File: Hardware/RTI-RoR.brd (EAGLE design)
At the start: 80 x 71.1 mm, 31 parts, among them IC2 74LVC244

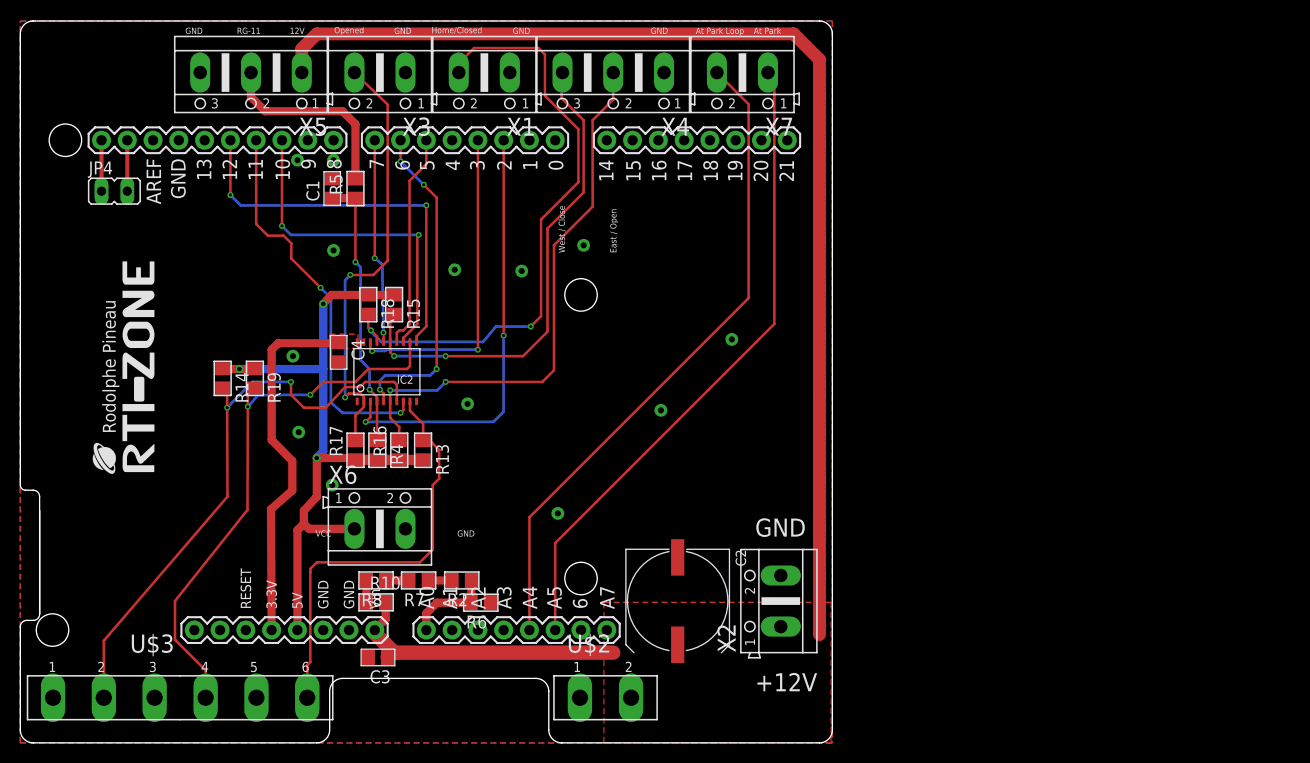
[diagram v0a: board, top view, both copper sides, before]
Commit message: Use the same board as the dome.
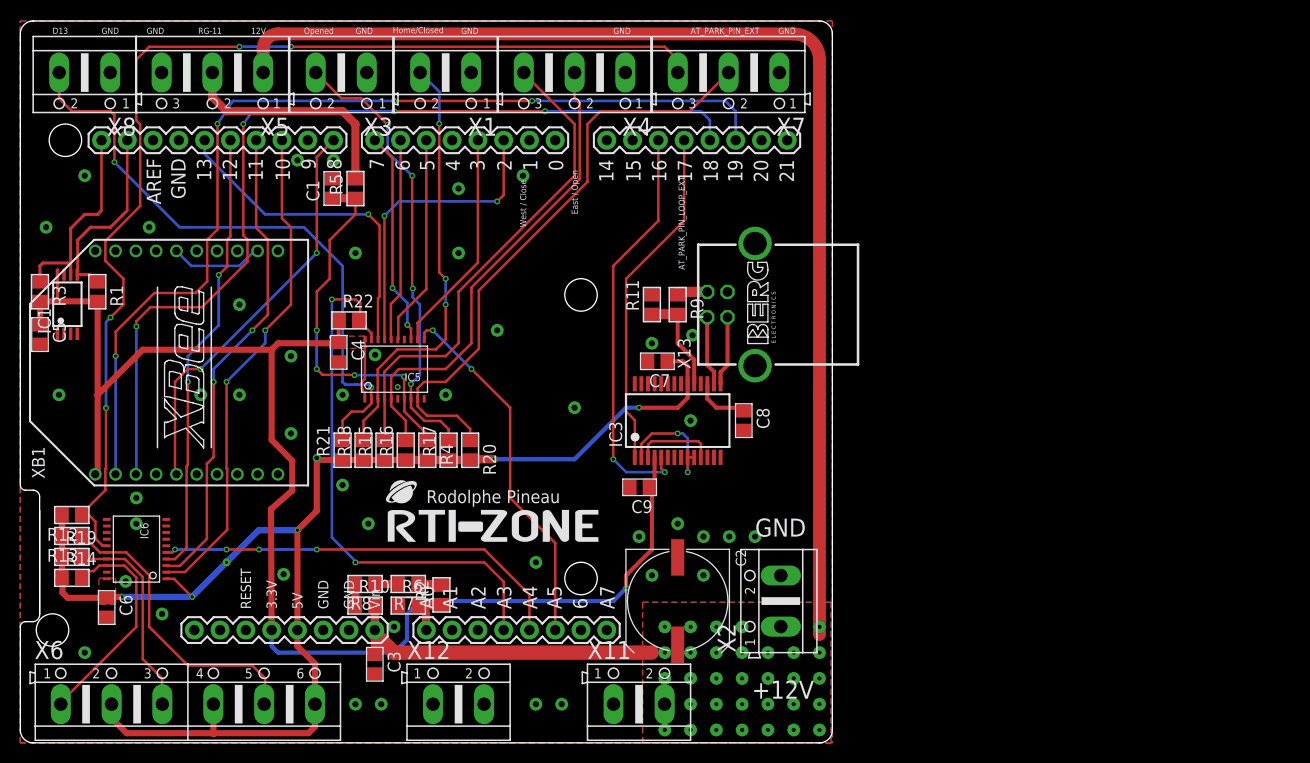
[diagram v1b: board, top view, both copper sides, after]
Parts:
- removed JP4: (no value), jumper:JP1
- removed U$2: STL-140-2, rti:STL-140-2
- removed U$3: STL-140-6, rti:STL-140-6
- added C5, C6, C7, C8, C9: 100nF, rti:C0805
- added IC1: 24AA128ST, microchip:TSSOP8
- added IC3: FT232RL, ftdichip:SSOP28
- added IC6: 74ABT245, rti:TSSOP20
- added R1, R3: 1K, rti:R0805
- added R11: 10K, rti:R0805
- added R12, R20, R21, R22, R9: 4.7K, rti:R0805
- added X11, X12, X8: (no value), con-ptr500:AK500/2
- added X13: PN61729-S, con-berg:PN61729-S
- added XB1: XBEE, maxstream:XBEE
- IC5: value 74LVC244 -> 74LVC245
- R13, R14, R19: value 1K -> 4.7K
- X6: device con-ptr500:AK500/2 -> con-ptr500:AK500/6
- X7: device con-ptr500:AK500/2 -> con-ptr500:AK500/3
- moved R13 35.6 mm to (5.08, 20.4), turned to 180 degrees
- moved X6 25.6 mm to (16.5, 3.81)
- moved R19 25.2 mm to (5.08, 18.3), turned to 0 degrees
- moved R14 24.6 mm to (5.08, 16.3), turned to 0 degrees
- moved U$4 24.0 mm to (36.2, 19.8), turned to 0 degrees
- moved R15 14.4 mm to (35.9, 28.8), turned to 90 degrees
- moved R18 14.4 mm to (33.8, 28.8), turned to 90 degrees
- moved R17 9.18 mm to (42.2, 28.8)
- moved R6 7.15 mm to (38.2, 13.5), turned to 0 degrees
- moved R4 4.92 mm to (40.1, 28.8)
- moved X1 3.81 mm to (41.9, 66.0)
- moved X4 3.81 mm to (54.6, 66.0)
- moved X5 3.81 mm to (18.9, 66.0)
- moved X3 3.81 mm to (31.6, 66.0)
- moved R2 2.46 mm to (41.5, 14.6), turned to 90 degrees
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- renumbered IC2 to IC5
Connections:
- removed net 13: PCB1.13
- removed net LOW_POWER: PCB1.4
- removed net N$8: JP4.2, PCB1.SDA1
- new net AT_PARK_PIN_EXT: IC5.P$9, R20.1, X7.2
- new net AT_PARK_PIN_LOOP_EXT: IC6.P$15, R12.1, X7.3
- new net BUF_EN: IC5.P$19, PCB1.A3, R22.2
- new net D13: IC5.P$18, PCB1.13
- new net D13_EXT: IC5.P$2, R21.2, X8.2
- new net DTR_DSR_DCD: IC3.10, IC3.2, IC3.9
- new net N$1: IC3.19, R11.1, R9.2
- new net N$4: IC5.P$14
- new net N$9: XB1.12, XB1.16
- new net RTS_CTS: IC3.11, IC3.3
- new net RX2: IC3.1, PCB1.17
- new net SCL: IC1.6, PCB1.SCL1, R3.1
- new net SDA: IC1.5, PCB1.SDA1, R1.1
- new net TX2: IC3.5, PCB1.16
- new net USBDM: IC3.16, X13.2
- new net USBDP: IC3.15, X13.3
- new net USB_VCC: R9.1, X13.1
- new net XBEE_DIN: PCB1.18, XB1.3
- new net XBEE_DOUT: PCB1.19, XB1.2
- net +12V: now also X11.2; no longer U$2.2
- net 3.3V: now also C5.1, C9.1, IC1.8, IC3.4, IC5.P$1, R1.2, R22.1, R3.2, XB1.1
- net AT_PARK_PIN: now also IC5.P$11; no longer X7.1
- net AT_PARK_PIN_LOOP: now also IC6.P$5; no longer X7.2
- net BUTTON_EAST_OPEN: now also IC5.P$15; no longer IC5.P$14
- net BUTTON_EAST_OPEN_5V: now also IC5.P$5; no longer IC5.P$6
- net BUTTON_WEST_CLOSE: now also IC5.P$16; no longer IC5.P$5
- net BUTTON_WEST_CLOSE_5V: now also IC5.P$4; no longer IC5.P$15
- net GND: now also C5.2, C6.2, C7.2, C8.2, C9.2, IC1.1, IC1.2, IC1.3, IC1.4, IC3.18, IC3.21, IC3.25, IC3.7, IC5.P$6, IC6.P$10, IC6.P$19, IC6.P$6, IC6.P$7, IC6.P$8, IC6.P$9, R11.2, X11.1, X12.1, X12.2, X13.4, X13.S1, X13.S2, X7.1, X8.1, XB1.10, XB1.9; no longer IC5.P$1, IC5.P$19, U$2.1, U$3.1, U$3.3, U$3.5, X6.2
- net HOME_SHUTTER_CLOSED: now also IC5.P$17; no longer IC5.P$3
- net HOME_SHUTTER_CLOSED_5V: now also IC5.P$3; no longer IC5.P$17
- net M_DIR: now also IC6.P$3; no longer IC5.P$8
- net M_DIR_5V: now also IC6.P$17, X6.3; no longer IC5.P$12, U$3.4
- net M_EN: now also IC6.P$2; no longer IC5.P$13
- net M_EN_5V: now also IC6.P$18, X6.1; no longer IC5.P$7, U$3.2
- net M_STEP: now also IC6.P$4; no longer IC5.P$11
- net M_STEP_5V: now also IC6.P$16, X6.5; no longer IC5.P$9, U$3.6
- net N$6: now also C8.1, IC3.17; no longer JP4.1, PCB1.SCL1
- net RG-11: now also IC5.P$13; no longer IC5.P$16
- net RG-11-IN_5V: now also IC5.P$7; no longer IC5.P$4
- net SHUTTER_OPENED: now also IC5.P$12; no longer IC5.P$18
- net SHUTTER_OPENED_5V: now also IC5.P$8; no longer IC5.P$2
- net VCC: now also C6.1, C7.1, IC3.20, IC6.P$1, IC6.P$20, R12.2, R20.2, R21.1, X6.2, X6.4, X6.6; no longer X6.1
- net XBEE_RESET: now also XB1.5
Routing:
- net 3.3V: track 36.4 -> 146.4 mm, vias 0 -> 1
- net AT_PARK_PIN_LOOP_EXT: track 0.00 -> 109.1 mm, vias 0 -> 4
- net XBEE_DOUT: track 0.00 -> 96.6 mm, vias 0 -> 4
- net XBEE_DIN: track 0.00 -> 91.2 mm, vias 0 -> 4
- net VCC: track 67.7 -> 135.2 mm, vias 3 -> 7
- net D13_EXT: track 0.00 -> 61.7 mm, vias 0 -> 2
- net AT_PARK_PIN_EXT: track 0.00 -> 59.3 mm
- net BUF_EN: track 0.00 -> 54.1 mm, vias 0 -> 2
- net TX2: track 0.00 -> 40.5 mm, vias 0 -> 2
- net XBEE_RESET: track 0.00 -> 40.2 mm, vias 0 -> 2
- net M_EN_5V: track 57.6 -> 21.9 mm, vias 2 -> 0
- net M_DIR_5V: track 54.6 -> 20.2 mm, vias 2 -> 0
- net RX2: track 0.00 -> 34.0 mm
- net D13: track 0.00 -> 32.8 mm, vias 0 -> 1
- net AT_PARK_PIN: track 64.1 -> 36.1 mm, vias 0 -> 2
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- added copper zone on layer 16, net +12V
- added copper zone on layer 1, net VCC
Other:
- outline, holes or cut-outs redrawn
- board text added: "AT_PARK_PIN_EXT"
- board text added: "AT_PARK_PIN_LOOP_EXT"
- board text added: "D13"
- board text removed: "At Park"
- board text removed: "At Park Loop"
- board text removed: "VCC"

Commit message: Re-base the code with the dome code
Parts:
- removed PCB1: ARDUINO_DUE_SHIELD_SHORT, arduino_shield:ARDUINO_DUE_SHIELD_SHORT
- removed R22, R9: 4.7K, rti:R0805
- removed X12: (no value), con-ptr500:AK500/2
- removed X6: (no value), con-ptr500:AK500/6
- added 25MHZ: CB3LV-OSCILATOR, rti:SMD-7050_4P
- added C10: 22nF, rcl:C0805
- added C11, C12, C14, C16, C17, C20: 100nF, rcl:C0805
- added C13, C18, C22: 10nF, rcl:C0805
- added C15, C21: 6.8nF, rcl:C0805
- added C19: 4.7uF, rcl:C0805
- added C25, C26: 10uF, rcl:C0805
- added FL1: BLM21AG121SN1D, BLM21AG121SN1D:L0805
- added IC4: REG1117, burr-brown:SOT223
- added J2: XT60PW-M, samacsys:XT60PWM
- added R23: 10 1%, rcl:R0805
- added R24, R25, R26, R27: 49.9 1%, rcl:R0805
- added R28, R29: 330, rcl:R0805
- added R30, R31, R32, R33, R34, R35, R36, R37, R38, R40: 4.7K, rcl:R0805
- added R39: 12.4K 1%, rcl:R0805
- added U$1: ARDUINO_DUE_SHIELD_FULL, arduino_shield:ARDUINO_DUE_SHIELD_FULL
- added U$2: MCP120T-270I_TT, MCP120T-270I_TT:SOT95P237X112-3N
- added U1: W5500, W5500:LQFP48
- added X10: (no value), rti:AK500/3
- added X9: J1011F21PNL, rti:J1011F21PNL
- C1, C3, C4, C5, C6, C7, C8, C9: device rti:C0805 -> rcl:C0805
- C2: device rti:UD-10X10_NICHICON -> rcl:UD-10X10_NICHICON
- IC1: device microchip:TSSOP8 -> rti:TSSOP8
- R1, R10, R11, R12, R13, R14, R15, R16, R17, R18, R19, R2, R20, R21, R3, R4, R5, R6, R7, R8: device rti:R0805 -> rcl:R0805
- X1, X11, X3, X8: device con-ptr500:AK500/2 -> rti:AK500/2
- X13: device con-berg:PN61729-S -> rti:PN61729-S
- X2: device con-ptr500:AK500/2 -> rti:AK500/3
- X4, X5, X7: device con-ptr500:AK500/3 -> rti:AK500/3
- XB1: device maxstream:XBEE -> rti:XBEE
- moved X2 66.7 mm to (8.99, 3.84), turned to 0 degrees
- moved IC3 45.5 mm to (106.7, 49.5)
- moved C7 45.5 mm to (104.7, 55.4)
- moved C8 45.5 mm to (113.2, 49.5)
- moved C9 45.5 mm to (102.9, 43.0)
- moved X13 45.5 mm to (114.3, 61.0)
- moved U$4 34.5 mm to (56.5, 47.8)
- moved R11 30.4 mm to (89.5, 56.7), turned to 0 degrees
- moved C2 29.5 mm to (94.0, 10.2)
- moved X11 21.6 mm to (82.5, 3.81)
- moved X7 1.02 mm to (68.8, 65.8)
- moved X4 0.85 mm to (53.8, 65.8)
- moved X1 0.64 mm to (41.3, 65.8)
- moved X3 0.38 mm to (31.3, 65.8)
- moved X5 0.24 mm to (18.8, 65.8)
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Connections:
- removed net BUF_EN: IC5.P$19, PCB1.A3, R22.2
- removed net N$1: IC3.19, R11.1, R9.2
- new net +3V3: 25MHZ.1, 25MHZ.4, C13.1, C16.1, C20.1, C26.1, C9.1, FL1.2, IC3.4, IC4.2, R28.2, R29.2, R30.2, R36.2, R37.2, R38.2, U1.28
- new net +5V: U$1.+5V@2
- new net ACT_LED: U1.27, X9.11
- new net AVDD: C11.1, C12.1, C14.1, C17.1, FL1.1, R23.2, R24.2, R25.2, U1.11, U1.15, U1.17, U1.21, U1.4, U1.8
- new net ETH_CS: U$1.52, U1.32
- new net ETH_RESET: R30.1, U$1.53, U1.37
- new net FTDI_RESET: IC3.19, R11.1, U$1.23
- new net INT_N: U$1.32, U1.36
- new net LINK_ACK: U1.25, X9.10
- new net N$10: R28.1, X9.12
- new net N$11: C15.2, X9.7
- new net N$12: C21.2, X9.8
- new net N$13: C10.1, R23.1, X9.3
- new net N$17: U1.26
- new net N$22: R31.1, U1.38
- new net N$23: R32.1, U1.39
- new net N$24: R33.1, U1.40
- new net N$25: R34.1, U1.41
- new net N$26: R35.1, U1.42
- new net N$27: R36.1, U1.43
- new net N$28: R37.1, U1.44
- new net N$29: R38.1, U1.45
- new net N$31: C19.2, U1.20
- new net N$32: U1.18
- new net N$33: C18.2, U1.22
- new net N$34: R39.1, U1.10
- new net N$35: R40.2, U1.23
- new net N$7: C22.1, R26.2, R27.2, X9.6
- new net N$8: R29.1, X9.9
- new net RESET: U$1.RESET, U$2.1
- new net RXN: C21.1, R26.1, U1.5
- new net RXP: C15.1, R27.1, U1.6
- new net SCLK: U$1.SCK, U1.33
- new net SDI: U$1.MISO, U1.34
- new net SDO: U$1.MOSI, U1.35
- new net TXN: R25.1, U1.1, X9.2
- new net TXP: R24.1, U1.2, X9.1
- new net XI: 25MHZ.3, U1.30
- new net XO: U1.31
- net +12V: now also C25.1, IC4.3, J2.2, U$1.VIN; no longer PCB1.VIN, X2.1
- net 3.3V: now also U$1.3.3V, U$2.2; no longer C9.1, IC3.4, PCB1.3.3V, R22.1
- net AT_PARK_PIN: now also U$1.A5; no longer PCB1.A5
- net AT_PARK_PIN_LOOP: now also U$1.A4; no longer PCB1.A4
- net BUTTON_EAST_OPEN: now also U$1.5; no longer PCB1.5
- net BUTTON_WEST_CLOSE: now also U$1.6; no longer PCB1.6
- net D13: now also U$1.13; no longer PCB1.13
- net GND: now also 25MHZ.2, C10.2, C11.2, C12.2, C13.2, C14.2, C16.2, C17.2, C18.1, C19.1, C20.2, C22.2, C25.2, C26.2, IC4.1, IC5.P$19, J2.1, R31.2, R32.2, R33.2, R34.2, R35.2, R39.2, R40.1, U$1.GND, U$1.GND., U$1.GND.., U$1.GND..., U$1.GND...., U$1.GND__, U$2.3, U1.14, U1.16, U1.19, U1.29, U1.3, U1.48, U1.9, X9.4, X9.5, X9.M1, X9.M2; no longer PCB1.GND, PCB1.GND., PCB1.GND.., X12.1, X12.2, X2.2
- net HOME_SHUTTER_CLOSED: now also U$1.2; no longer PCB1.2
- net M_DIR: now also U$1.11; no longer PCB1.11
- net M_DIR_5V: now also X2.3; no longer X6.3
- net M_EN: now also U$1.10; no longer PCB1.10
- net M_EN_5V: now also X2.1; no longer X6.1
- net M_STEP: now also U$1.12; no longer PCB1.12
- net M_STEP_5V: now also X10.2; no longer X6.5
- net RG-11: now also U$1.7; no longer PCB1.7
- net RX2: now also U$1.17; no longer PCB1.17
- net SCL: now also U$1.SCL1; no longer PCB1.SCL1
- net SDA: now also U$1.SDA1; no longer PCB1.SDA1
- net SHUTTER_OPENED: now also U$1.3; no longer PCB1.3
- net TX2: now also U$1.16; no longer PCB1.16
- net USB_VCC: no longer R9.1
- net VCC: now also U$1.+5V@1, U$1.+5V@3, U$1.+5V@4, X10.1, X10.3, X2.2; no longer PCB1.5V, X6.2, X6.4, X6.6
- net VPIN: now also U$1.A0; no longer PCB1.A0
- net XBEE_DIN: now also U$1.18; no longer PCB1.18
- net XBEE_DOUT: now also U$1.19; no longer PCB1.19
- net XBEE_RESET: now also U$1.8; no longer PCB1.8
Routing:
- net +3V3: track 0.00 -> 146.7 mm
- net AVDD: track 0.00 -> 96.8 mm, vias 0 -> 4
- net +12V: track 148.7 -> 239.2 mm
- net 3.3V: track 146.4 -> 90.1 mm, vias 1 -> 0
- net BUF_EN: track 54.1 -> 0.00 mm, vias 2 -> 0
- net ACT_LED: track 0.00 -> 48.9 mm, vias 0 -> 1
- net ETH_RESET: track 0.00 -> 46.6 mm, vias 0 -> 1
- net LINK_ACK: track 0.00 -> 45.7 mm, vias 0 -> 1
- net INT_N: track 0.00 -> 43.4 mm
- net TXN: track 0.00 -> 39.7 mm
- net TXP: track 0.00 -> 39.4 mm
- net N$7: track 0.00 -> 30.8 mm, vias 0 -> 3
- net FTDI_RESET: track 0.00 -> 29.7 mm, vias 0 -> 1
- net RXN: track 0.00 -> 27.6 mm, vias 0 -> 2
- net RXP: track 0.00 -> 27.4 mm, vias 0 -> 2
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- added copper zone on layer 1, net +3V3
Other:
- board size 80 x 71.1 mm -> 119.4 x 71.2 mm
- board text added: "+5V"
- board text added: "DIR"
- board text added: "Dome Rotator"
- board text added: "EN"
- board text added: "East"
- board text added: "Home"
- board text added: "STEP"
- board text added: "West"
- board text removed: "East / Open"
- board text removed: "Home/Closed"
- board text removed: "West / Close"
